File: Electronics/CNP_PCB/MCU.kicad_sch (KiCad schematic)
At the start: 1 part, among them U1 ESP32-C3

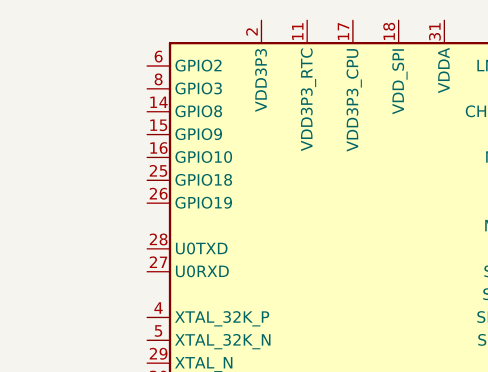
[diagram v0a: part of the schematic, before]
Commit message: Latch circuit changes
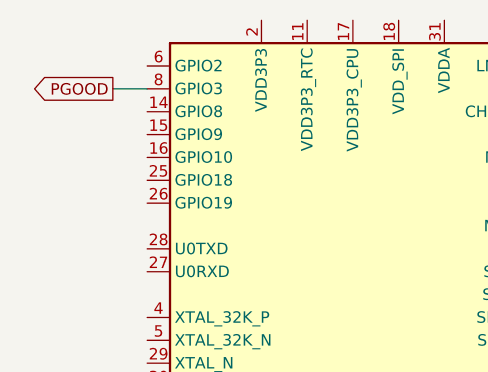
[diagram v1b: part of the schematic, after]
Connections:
- net PGOOD: now reaches U1.8 (GPIO3)
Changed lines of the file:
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@@
 	(generator_version "9.0")
 	(paper "A4")
+	(wire
+		(pts
+			(xy 170.18 55.88) (xy 173.99 55.88)
+		)
+		(stroke
+			(width 0)
+			(type default)
+		)
+	)
+	(global_label "PGOOD"
+		(shape output)
+		(at 170.18 55.88 180)
+		(fields_autoplaced yes)
+		(effects
+			(font
+				(size 1.27 1.27)
+			)
+			(justify right)
+		)
+		(property "Intersheetrefs" "${INTERSHEET_REFS}"
+			(at 160.7238 55.88 0)
+			(effects
+				(font
+					(size 1.27 1.27)
+				)
+				(justify right)
+				(hide yes)
+			)
+		)
+	)
 	(symbol
 		(lib_id "MCU_Espressif:ESP32-C3")

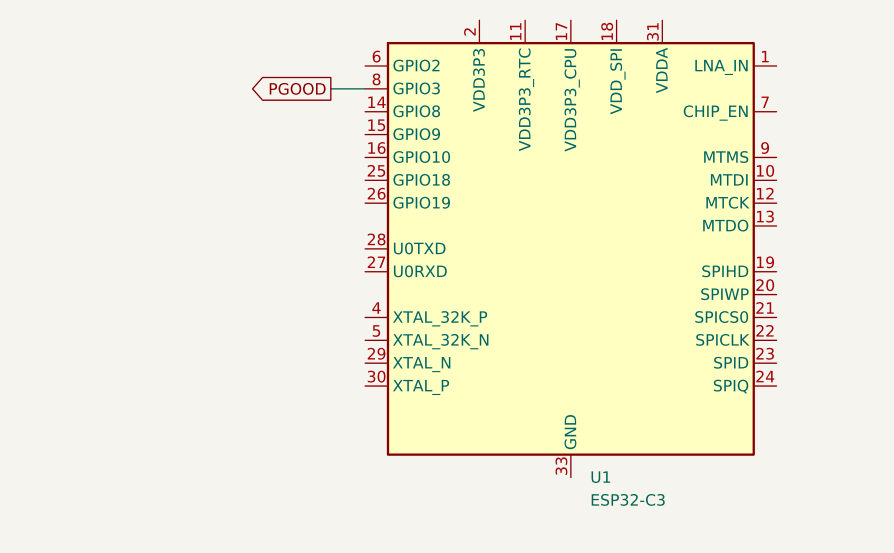
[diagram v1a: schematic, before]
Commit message: added switch logic for emulating buttons
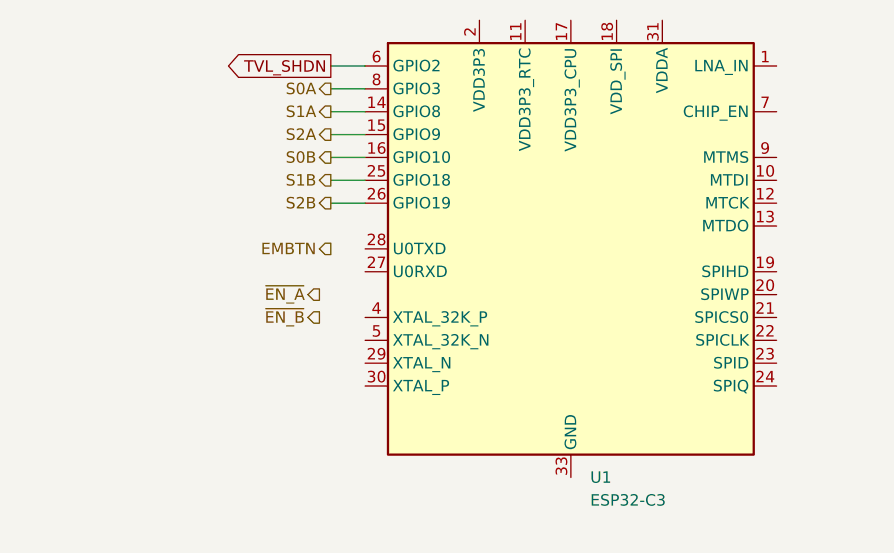
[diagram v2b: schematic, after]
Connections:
- net S1A: now reaches U1.14 (GPIO8)
- net S2A: now reaches U1.15 (GPIO9)
- net S0B: now reaches U1.16 (GPIO10)
- net S1B: now reaches U1.25 (GPIO18)
- net S2B: now reaches U1.26 (GPIO19)
- net TVL_SHDN: now reaches U1.6 (GPIO2)
- net PGOOD renamed S0A
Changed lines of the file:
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@@
+	(wire
+		(pts
+			(xy 170.18 68.58) (xy 173.99 68.58)
+		)
+		(stroke
+			(width 0)
+			(type default)
+		)
+	)
+	(wire
+		(pts
+			(xy 170.18 58.42) (xy 173.99 58.42)
+		)
+		(stroke
+			(width 0)
+			(type default)
+		)
+	)
+	(wire
+		(pts
+			(xy 170.18 60.96) (xy 173.99 60.96)
+		)
+		(stroke
+			(width 0)
+			(type default)
+		)
+	)
+	(wire
+		(pts
+			(xy 170.18 66.04) (xy 173.99 66.04)
+		)
+		(stroke
+			(width 0)
+			(type default)
+		)
+	)
 	(wire
 		(pts
@@
 		)
 	)
-	(global_label "PGOOD"
+	(wire
+		(pts
+			(xy 170.18 63.5) (xy 173.99 63.5)
+		)
+		(stroke
+			(width 0)
+			(type default)
+		)
+	)
+	(wire
+		(pts
+			(xy 170.18 53.34) (xy 173.99 53.34)
+		)
+		(stroke
+			(width 0)
+			(type default)
+		)
+	)
+	(global_label "TVL_SHDN"
 		(shape output)
-		(at 170.18 55.88 180)
+		(at 170.18 53.34 180)
 		(fields_autoplaced yes)
 		(effects
@@
 		)
 		(property "Intersheetrefs" "${INTERSHEET_REFS}"
-			(at 160.7238 55.88 0)
+			(at 158.0024 53.34 0)
 			(effects
 				(font
@@
 		)
 	)
+	(hierarchical_label "S2B"
+		(shape output)
+		(at 170.18 68.58 180)
+		(effects
+			(font
+				(size 1.27 1.27)
+			)
+			(justify right)
+		)
+	)
+	(hierarchical_label "~{EN_A}"
+		(shape output)
+		(at 168.91 78.74 180)
+		(effects
+			(font
+				(size 1.27 1.27)
+			)
+			(justify right)
+		)
+	)
+	(hierarchical_label "EMBTN"
+		(shape output)
+		(at 170.18 73.66 180)
+		(effects
+			(font
+				(size 1.27 1.27)
+			)
+			(justify right)
+		)
+	)
+	(hierarchical_label "S1B"
+		(shape output)
+		(at 170.18 66.04 180)
+		(effects
+			(font
+				(size 1.27 1.27)
+			)
+			(justify right)
+		)
+	)
+	(hierarchical_label "~{EN_B}"
+		(shape output)
+		(at 168.91 81.28 180)
+		(effects
+			(font
+				(size 1.27 1.27)
+			)
+			(justify right)
+		)
+	)
+	(hierarchical_label "S0A"
+		(shape output)
+		(at 170.18 55.88 180)
+		(effects
+			(font
+				(size 1.27 1.27)
+			)
+			(justify right)
+		)
+	)
+	(hierarchical_label "S2A"
+		(shape output)
+		(at 170.18 60.96 180)
+		(effects
+			(font
+				(size 1.27 1.27)
+			)
+			(justify right)
+		)
+	)
+	(hierarchical_label "S1A"
+		(shape output)
+		(at 170.18 58.42 180)
+		(effects
+			(font
+				(size 1.27 1.27)
+			)
+			(justify right)
+		)
+	)
+	(hierarchical_label "S0B"
+		(shape output)
+		(at 170.18 63.5 180)
+		(effects
+			(font
+				(size 1.27 1.27)
+			)
+			(justify right)
+		)
+	)

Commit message: changes made to button read logic
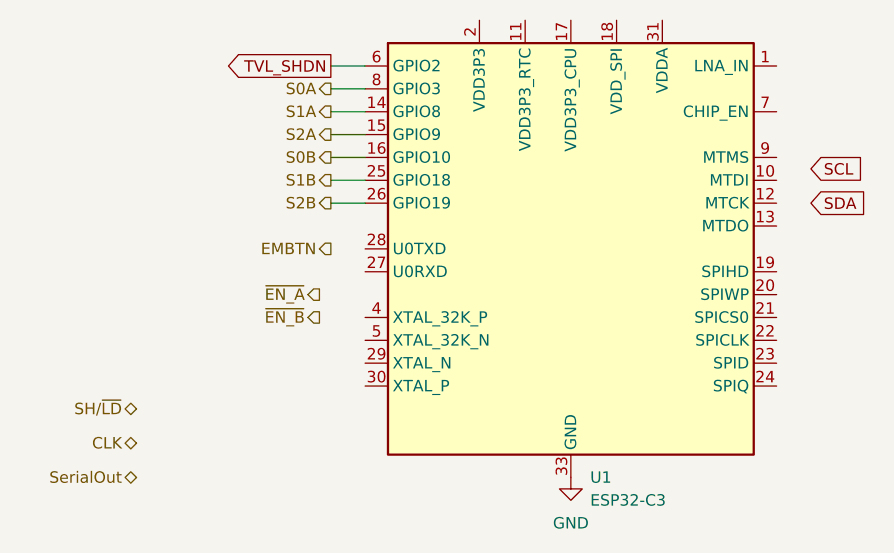
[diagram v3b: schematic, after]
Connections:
- net GND: now reaches U1.33 (GND)
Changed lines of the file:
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@@
+		)
+	)
+	(global_label "SCL"
+		(shape input)
+		(at 223.52 64.77 0)
+		(fields_autoplaced yes)
+		(effects
+			(font
+				(size 1.27 1.27)
+			)
+			(justify left)
+		)
+		(property "Intersheetrefs" "${INTERSHEET_REFS}"
+			(at 230.0128 64.77 0)
+			(effects
+				(font
+					(size 1.27 1.27)
+				)
+				(justify left)
+				(hide yes)
+			)
 		)
 	)
@@
 		)
 	)
+	(global_label "SDA"
+		(shape input)
+		(at 223.52 68.58 0)
+		(fields_autoplaced yes)
+		(effects
+			(font
+				(size 1.27 1.27)
+			)
+			(justify left)
+		)
+		(property "Intersheetrefs" "${INTERSHEET_REFS}"
+			(at 230.0733 68.58 0)
+			(effects
+				(font
+					(size 1.27 1.27)
+				)
+				(justify left)
+				(hide yes)
+			)
+		)
+	)
 	(hierarchical_label "S2B"
 		(shape output)
@@
 		)
 	)
+	(hierarchical_label "SH{slash}~{LD}"
+		(shape bidirectional)
+		(at 148.59 91.44 180)
+		(effects
+			(font
+				(size 1.27 1.27)
+			)
+			(justify right)
+		)
+	)
 	(hierarchical_label "EMBTN"
 		(shape output)
@@
 		)
 	)
+	(hierarchical_label "CLK"
+		(shape bidirectional)
+		(at 148.59 95.25 180)
+		(effects
+			(font
+				(size 1.27 1.27)
+			)
+			(justify right)
+		)
+	)
 	(hierarchical_label "S1B"
 		(shape output)
@@
 		(shape output)
 		(at 168.91 81.28 180)
+		(effects
+			(font
+				(size 1.27 1.27)
+			)
+			(justify right)
+		)
+	)
+	(hierarchical_label "SerialOut"
+		(shape bidirectional)
+		(at 148.59 99.06 180)
 		(effects
 			(font
@@
 					(unit 1)
 				)
+			)
+		)
+	)
+	(symbol
+		(lib_id "power:GND")
+		(at 196.85 99.06 0)
+		(unit 1)
+		(exclude_from_sim no)
+		(in_bom yes)
+		(on_board yes)
+		(dnp no)
+		(fields_autoplaced yes)
+		(property "Reference" "#PWR013"
+			(at 196.85 105.41 0)
+			(effects
+				(font
+					(size 1.27 1.27)
+				)
+				(hide yes)
+			)
+		)
+		(property "Value" "GND"
+			(at 196.85 104.14 0)
+			(effects
+				(font
+					(size 1.27 1.27)
+				)
+			)
+		)
+		(property "Footprint" ""
+			(at 196.85 99.06 0)
+			(effects
+				(font
+					(size 1.27 1.27)
+				)
+				(hide yes)
+			)
+		)
+		(property "Datasheet" ""
+			(at 196.85 99.06 0)
+			(effects
+				(font
+					(size 1.27 1.27)
+				)
+				(hide yes)
+			)
+		)
+		(property "Description" "Power symbol creates a global label with name \"GND\" , ground"
+			(at 196.85 99.06 0)
+			(effects
+				(font
+					(size 1.27 1.27)
+				)
+				(hide yes)
+			)
+		)
+		(pin "1"
+		)
+		(instances
+			(project ""
+				(path "/3fdafdbf-442b-4f7c-b60a-a85895f9231b/d1ebdc37-c3ca-4f02-99ba-91c32b1fdbe2"
+					(reference "#PWR013")
+					(unit 1)
+				)
